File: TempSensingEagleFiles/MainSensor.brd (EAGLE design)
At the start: 40 x 40 mm, 14 parts, among them U3 MLX90614_

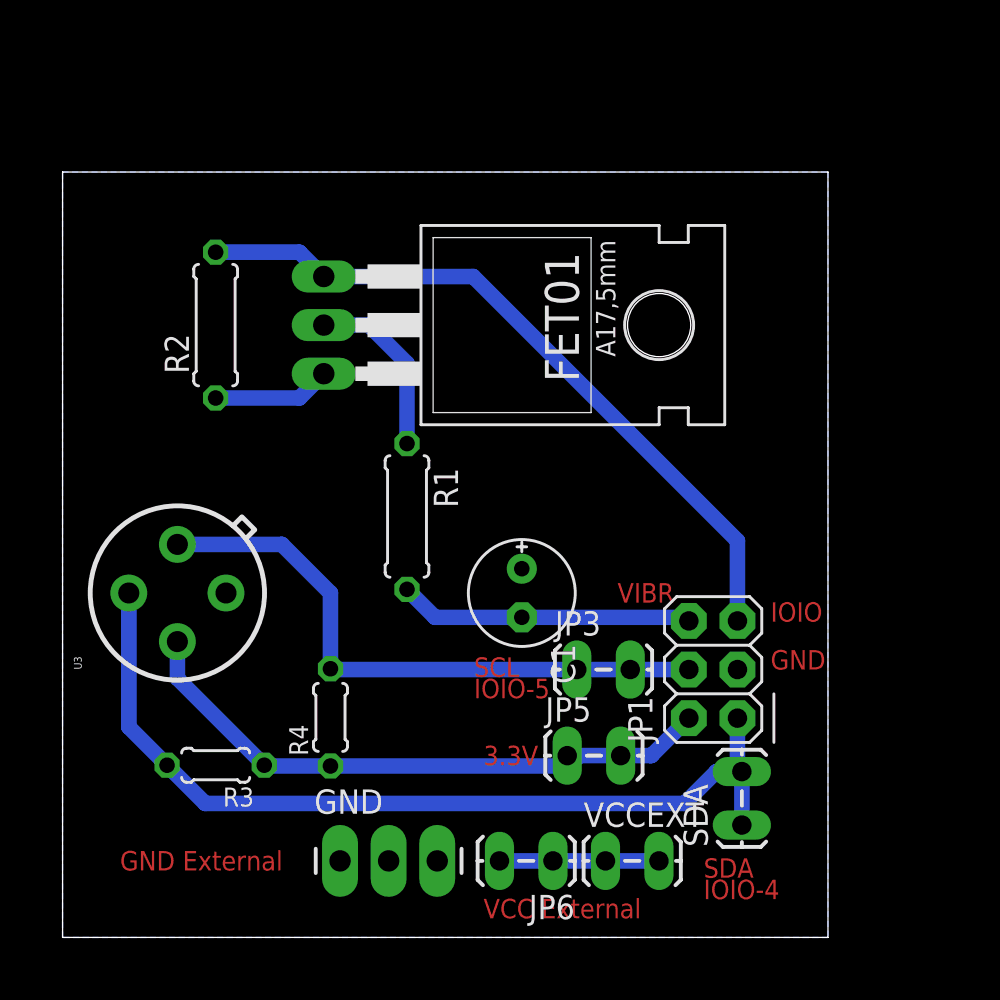
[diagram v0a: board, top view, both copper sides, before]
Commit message: worked on Eagle Files
Added 1 Sensor and Main board
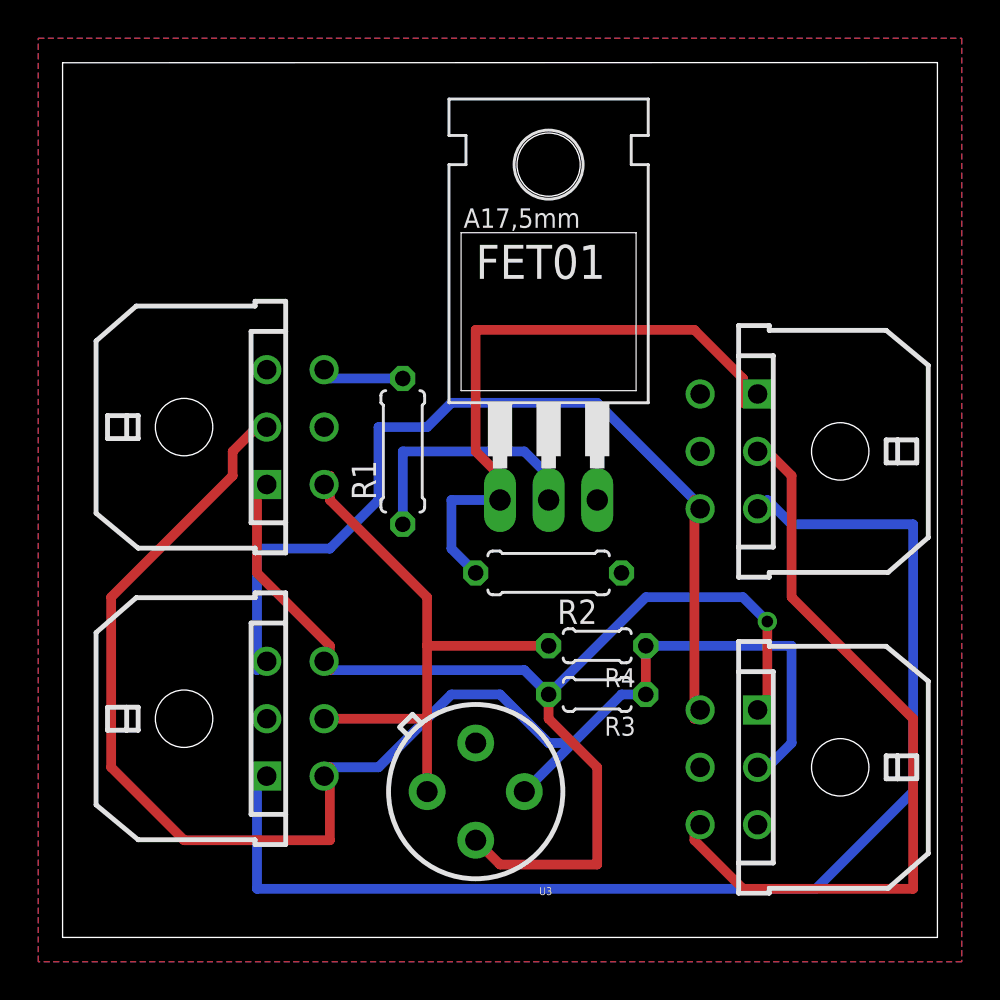
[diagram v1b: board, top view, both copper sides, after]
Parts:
- removed C1: 47uf, rcl:E2,5-6E
- removed GND: (no value), SparkFun-Connectors:1X03_LONGPADS
- removed JP1: (no value), SparkFun-Connectors:2X03
- removed JP3, JP5, JP6, SDA, VCCEXT: (no value), SparkFun-Connectors:1X02_LOCK_LONGPADS
- added 9V, IOIO, LEFT, RIGHT: (no value), con-molex-micro-fit-3_0:43045-0600
- moved R2 21.7 mm to (25.4, 19.1), turned to 180 degrees
- moved R3 20.3 mm to (27.9, 12.7)
- moved U3 18.7 mm to (21.6, 7.62), turned to 180 degrees
- moved R4 14.4 mm to (27.9, 15.2), turned to 180 degrees
- moved FET01 6.08 mm to (25.4, 29.2), turned to 0 degrees
- moved R1 3.41 mm to (17.8, 25.4), turned to 90 degrees
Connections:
- new net N$4: 9V.P$3, LEFT.P$1
- new net VCC: 9V.P$6, LEFT.P$3, RIGHT.P$4
- net GND: now also IOIO.P$3, LEFT.P$2, RIGHT.P$5; no longer C1.+, GND.1, GND.2, GND.3, JP1.3
- net N$1: now also 9V.P$2, RIGHT.P$6; no longer JP6.1, JP6.2, VCCEXT.1, VCCEXT.2
- net N$15: now also IOIO.P$4, LEFT.P$5; no longer JP1.4, JP3.1, JP3.2
- net N$16: now also IOIO.P$1, LEFT.P$6, RIGHT.P$1; no longer JP1.1, SDA.1, SDA.2
- net N$18: now also 9V.P$1; no longer JP1.5
- net N$3: now also IOIO.P$6; no longer C1.-, JP1.6
- net VCC3: now also IOIO.P$2, LEFT.P$4, RIGHT.P$2; no longer JP1.2, JP5.1, JP5.2
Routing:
- net N$4: track 0.00 -> 66.2 mm
- net VCC: track 0.00 -> 50.5 mm
- net VCC3: track 32.2 -> 80.7 mm
- net N$1: track 8.33 -> 40.8 mm
- net N$16: track 47.1 -> 62.1 mm, vias 0 -> 1
- net N$3: track 15.4 -> 4.36 mm
- net GND: track 6.46 -> 0.00 mm
- net N$18: track 37.7 -> 33.5 mm
- net N$2: track 9.37 -> 13.2 mm
- net N$15: track 31.8 -> 30.9 mm
- added copper zone on layer 1, net GND
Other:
- board size 40 x 40 mm -> 45.7 x 45.7 mm
- board text removed: "3.3V"
- board text removed: "GND"
- board text removed: "GND External"
- board text removed: "IOIO"
- board text removed: "SCL IOIO-5"
- board text removed: "SDA IOIO-4"
- board text removed: "VCC External"
- board text removed: "VIBR"

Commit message: STABLE: Added better threading
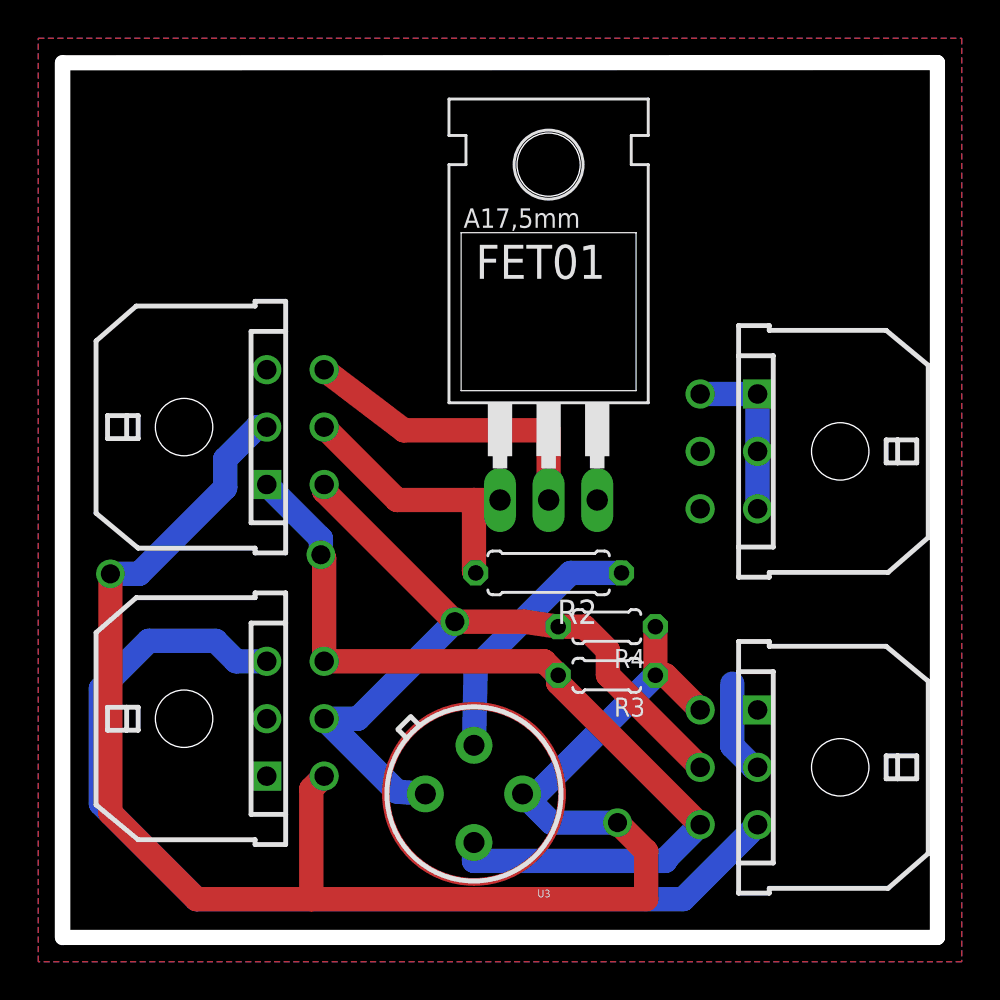
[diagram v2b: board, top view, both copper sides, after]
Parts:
- removed R1: 10h, rcl:0207/7
- moved R3 1.12 mm to (28.4, 13.7)
- moved R4 1.12 mm to (28.4, 16.2)
- moved U3 0.15 mm to (21.5, 7.50)
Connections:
- removed net N$15: IOIO.P$4, LEFT.P$5, R4.2, U3.1
- removed net N$16: IOIO.P$1, LEFT.P$6, R3.2, RIGHT.P$1, U3.2
- removed net N$18: 9V.P$1, FET01.B, R2.2
- removed net N$2: FET01.C, R1.1
- removed net N$3: IOIO.P$6, R1.2
- removed net N$4: 9V.P$3, LEFT.P$1
- removed net VCC3: IOIO.P$2, LEFT.P$4, R3.1, R4.1, RIGHT.P$2, U3.3
- new net 3.3V: IOIO.P$2, LEFT.P$4, R3.1, R4.1, RIGHT.P$4, U3.3
- new net IOIOPIN: FET01.B, IOIO.P$5, R2.2
- new net SCL: IOIO.P$4, LEFT.P$5, R4.2, RIGHT.P$5, U3.1
- new net SDA: IOIO.P$1, LEFT.P$6, R3.2, RIGHT.P$6, U3.2
- new net VIB: FET01.C, IOIO.P$6
- net GND: now also 9V.P$5, RIGHT.P$2; no longer RIGHT.P$5
- net N$1: now also 9V.P$1, 9V.P$3, 9V.P$4; no longer RIGHT.P$6
- net VCC: now also RIGHT.P$3; no longer 9V.P$6, RIGHT.P$4
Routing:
- net 3.3V: track 0.00 -> 86.6 mm, vias 0 -> 2
- net VCC3: track 80.7 -> 0.00 mm
- net N$4: track 66.2 -> 0.00 mm
- net N$16: track 62.1 -> 0.00 mm, vias 1 -> 0
- net SDA: track 0.00 -> 47.5 mm, vias 0 -> 1
- net SCL: track 0.00 -> 42.4 mm, vias 0 -> 1
- net N$18: track 33.5 -> 0.00 mm
- net N$1: track 40.8 -> 9.00 mm
- net N$15: track 30.9 -> 0.00 mm
- net GND: track 0.00 -> 18.8 mm
- net VIB: track 0.00 -> 16.4 mm
- net IOIOPIN: track 0.00 -> 14.6 mm
- net N$2: track 13.2 -> 0.00 mm
- net N$3: track 4.36 -> 0.00 mm
- net VCC: track 50.5 -> 54.2 mm

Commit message: Revert "STABLE: Added better threading"
This reverts commit b74bb6b943322a5487aef219e170d9d2f1191ec7.
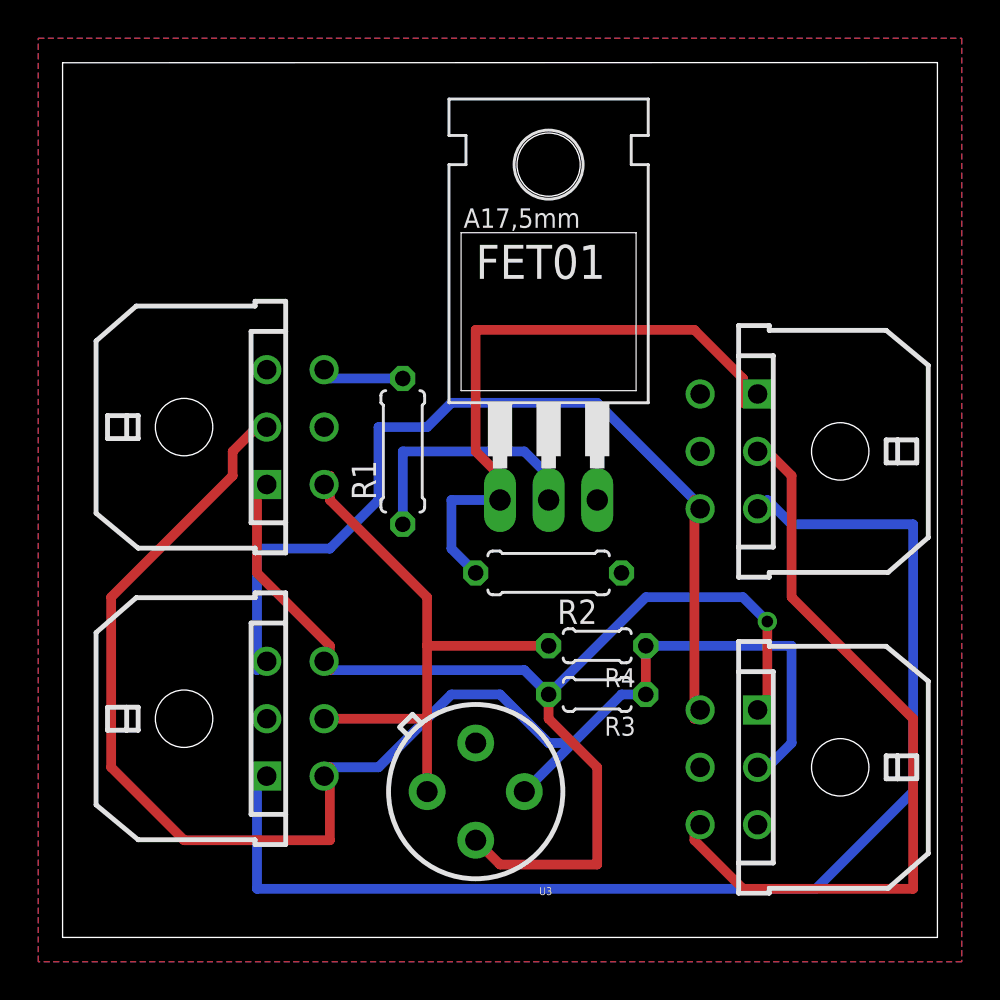
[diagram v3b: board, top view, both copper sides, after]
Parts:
- added R1: 10h, rcl:0207/7
- moved R3 1.12 mm to (27.9, 12.7)
- moved R4 1.12 mm to (27.9, 15.2)
- moved U3 0.15 mm to (21.6, 7.62)
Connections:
- removed net 3.3V: IOIO.P$2, LEFT.P$4, R3.1, R4.1, RIGHT.P$4, U3.3
- removed net IOIOPIN: FET01.B, IOIO.P$5, R2.2
- removed net SCL: IOIO.P$4, LEFT.P$5, R4.2, RIGHT.P$5, U3.1
- removed net SDA: IOIO.P$1, LEFT.P$6, R3.2, RIGHT.P$6, U3.2
- removed net VIB: FET01.C, IOIO.P$6
- new net N$15: IOIO.P$4, LEFT.P$5, R4.2, U3.1
- new net N$16: IOIO.P$1, LEFT.P$6, R3.2, RIGHT.P$1, U3.2
- new net N$18: 9V.P$1, FET01.B, R2.2
- new net N$2: FET01.C, R1.1
- new net N$3: IOIO.P$6, R1.2
- new net N$4: 9V.P$3, LEFT.P$1
- new net VCC3: IOIO.P$2, LEFT.P$4, R3.1, R4.1, RIGHT.P$2, U3.3
- net GND: now also RIGHT.P$5; no longer 9V.P$5, RIGHT.P$2
- net N$1: now also RIGHT.P$6; no longer 9V.P$1, 9V.P$3, 9V.P$4
- net VCC: now also 9V.P$6, RIGHT.P$4; no longer RIGHT.P$3
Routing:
- net 3.3V: track 86.6 -> 0.00 mm, vias 2 -> 0
- net VCC3: track 0.00 -> 80.7 mm
- net N$4: track 0.00 -> 66.2 mm
- net N$16: track 0.00 -> 62.1 mm, vias 0 -> 1
- net SDA: track 47.5 -> 0.00 mm, vias 1 -> 0
- net SCL: track 42.4 -> 0.00 mm, vias 1 -> 0
- net N$18: track 0.00 -> 33.5 mm
- net N$1: track 9.00 -> 40.8 mm
- net N$15: track 0.00 -> 30.9 mm
- net GND: track 18.8 -> 0.00 mm
- net VIB: track 16.4 -> 0.00 mm
- net IOIOPIN: track 14.6 -> 0.00 mm
- net N$2: track 0.00 -> 13.2 mm
- net N$3: track 0.00 -> 4.36 mm
- net VCC: track 54.2 -> 50.5 mm
